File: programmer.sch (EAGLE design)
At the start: 26 parts, among them IC1 74241, U1 ATMEGA8U2, X2 SPARKFUN_USB-MICROB, Y1 16MHz

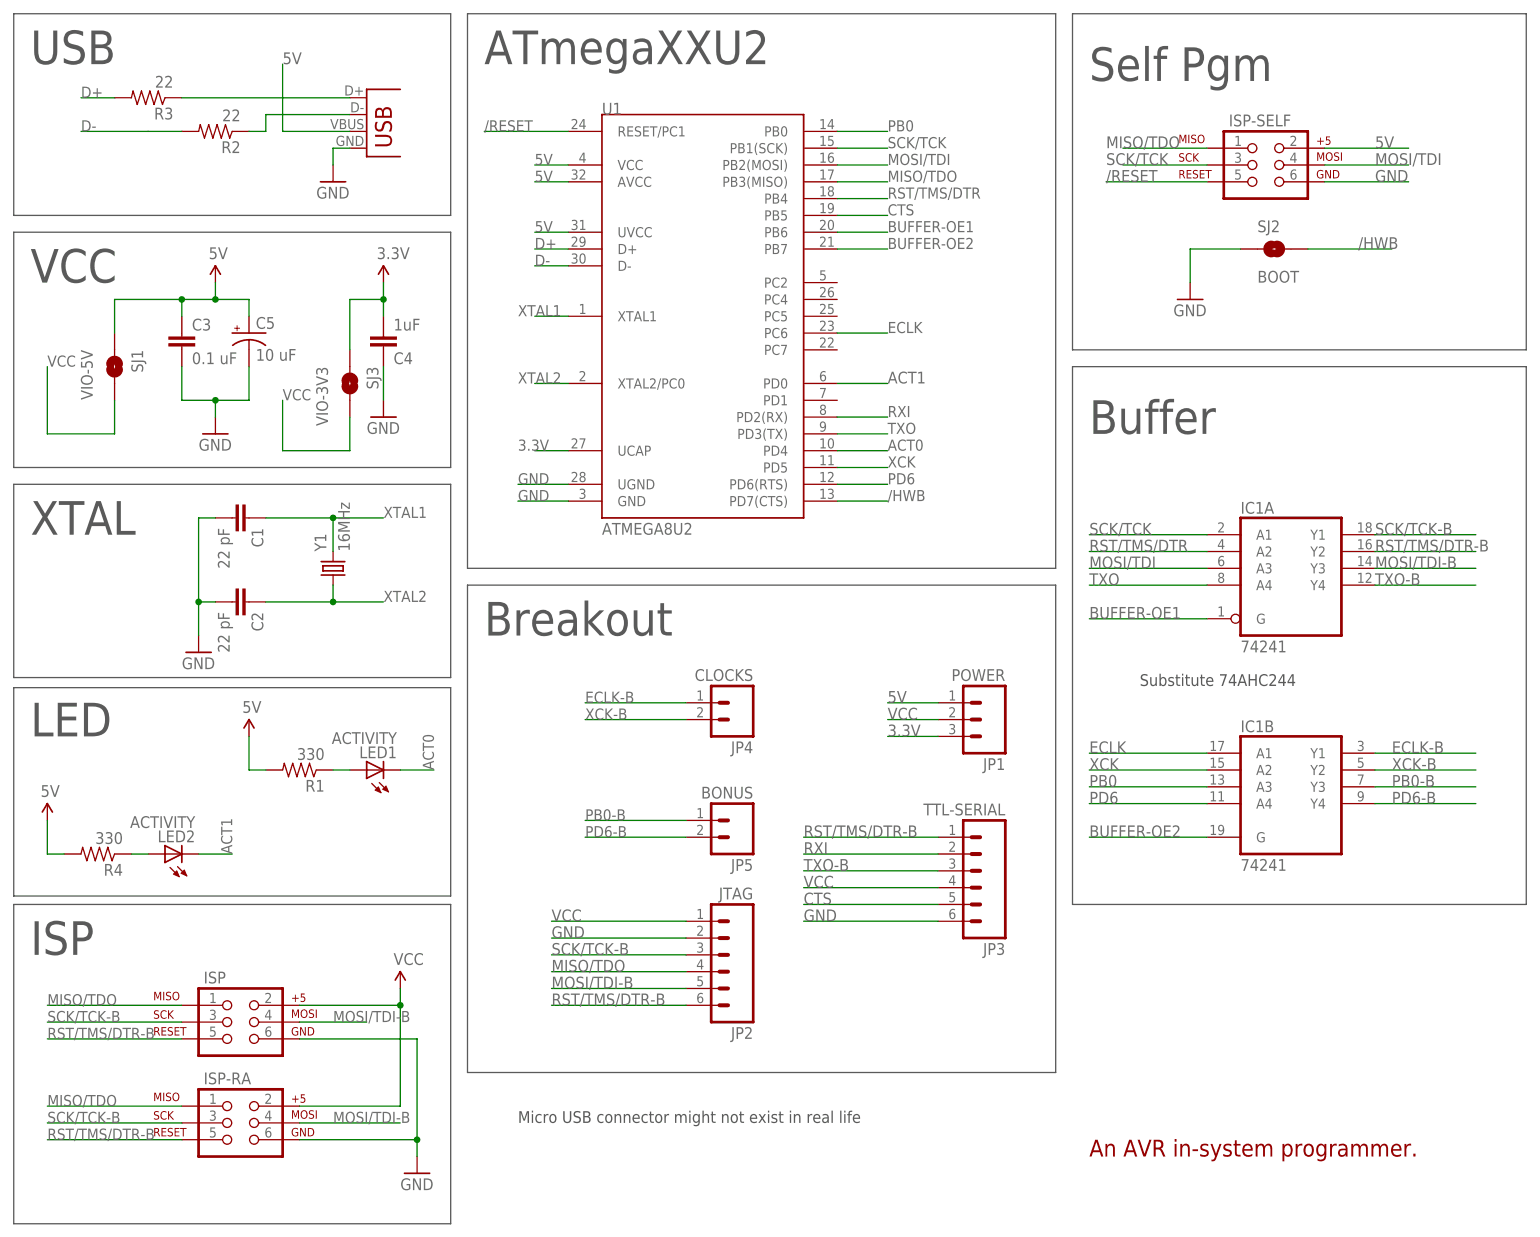
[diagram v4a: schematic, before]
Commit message: Added switch.
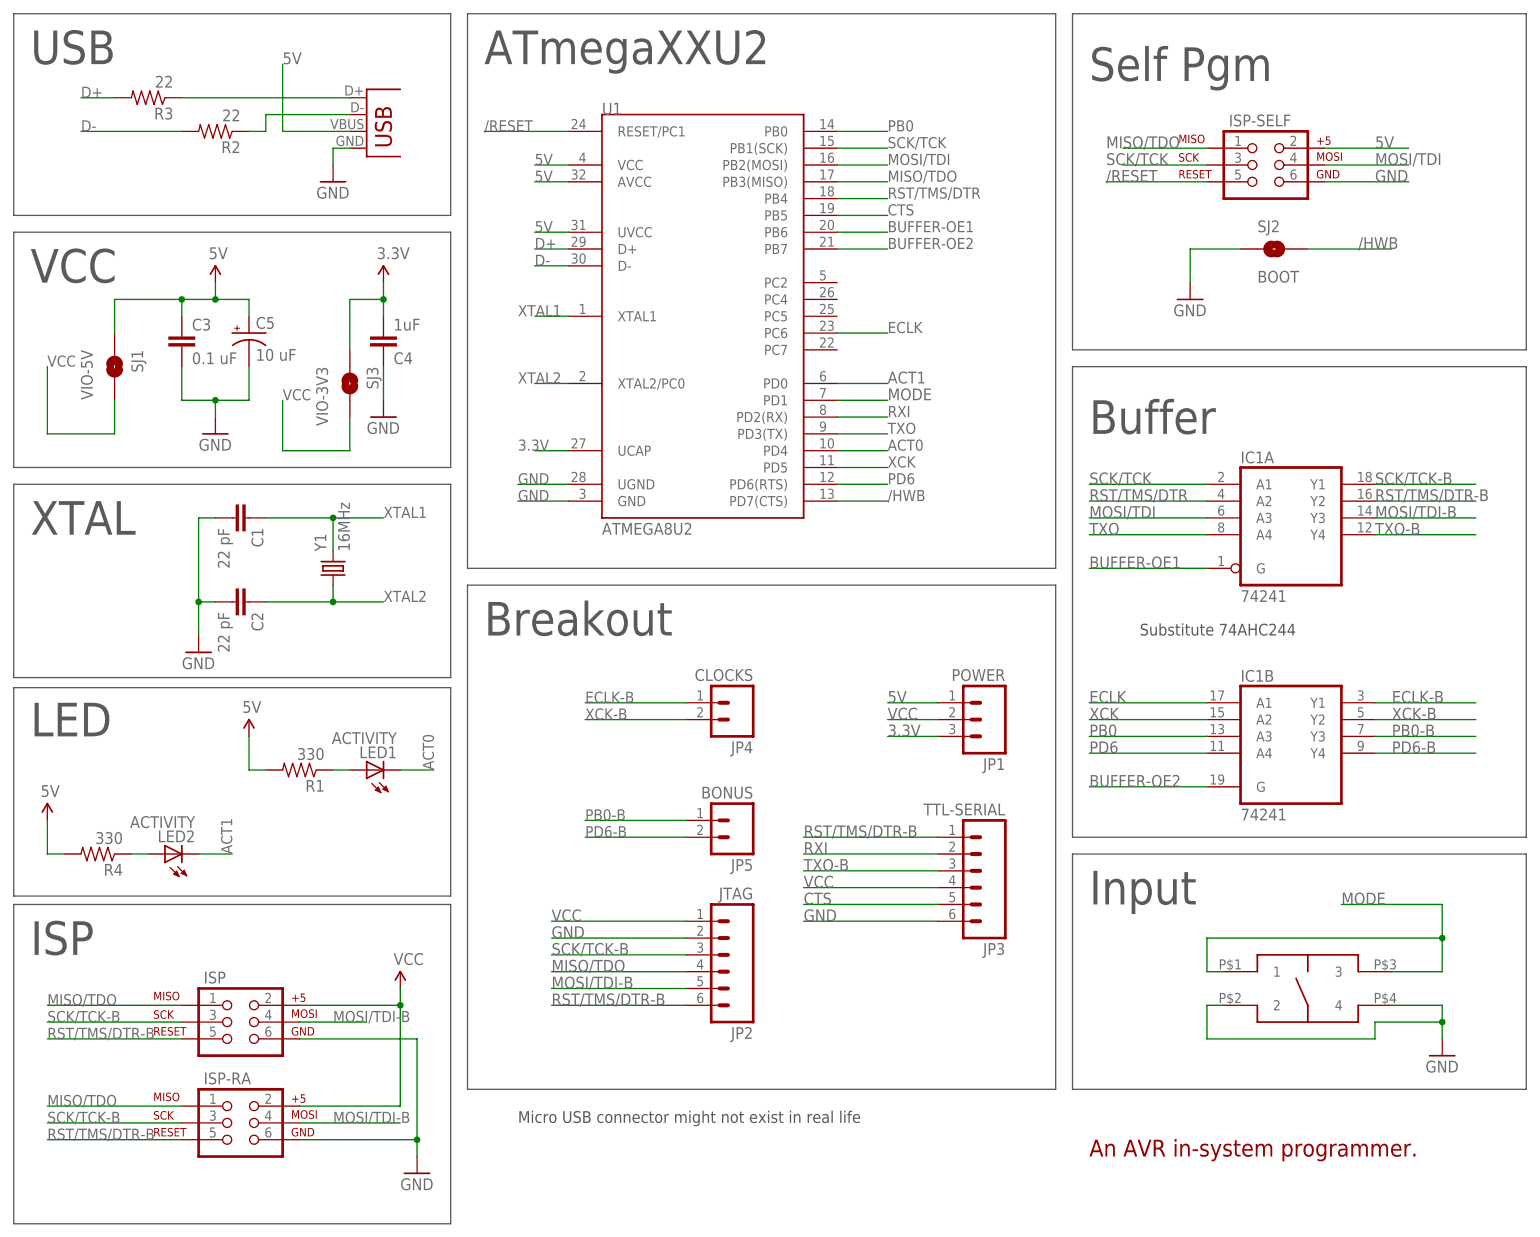
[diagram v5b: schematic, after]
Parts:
- added U$4: MOUNTAIN-MS-100625, programmer:MOUNTAIN-MS-100625
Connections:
- new net MODE: U$4.1, U$4.3, U1.PD1
- net GND: now also U$4.2, U$4.4
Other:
- note added: "Input"
- moved on the sheet: IC1A, IC1B

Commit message: Add FCI 10118193 USB socket.
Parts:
- removed X2: SPARKFUN_USB-MICROB, programmer:SPARKFUN_USB-MICROB
- added X1: FCI_8193_MICRO_USB, programmer:FCI_8193_MICRO_USB
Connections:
- net 5V: now also X1.VBUS; no longer X2.VBUS
- net D+RAW: now also X1.D+; no longer X2.D+
- net D-RAW: now also X1.D-; no longer X2.D-
- net GND: now also X1.GND; no longer X2.GND
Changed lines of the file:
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@@
 <part name="ISP-RA" library="programmer" deviceset="SPARKFUN_AVR_SPI_PRG_6" device="2X3_LOCK" value=""/>
 <part name="ISP-SELF" library="programmer" deviceset="SPARKFUN_AVR_SPI_PRG_6" device="2X3_LOCK" value=""/>
-<part name="X2" library="programmer" deviceset="SPARKFUN_USB" device="-MICROB"/>
 <part name="SJ1" library="programmer" deviceset="SPARKFUN_SOLDERJUMPER" device="NC" value="VIO-5V"/>
 <part name="JP2" library="programmer" deviceset="SPARKFUN_M06" device="LOCK" value="JTAG"/>
@@
 <part name="U$4" library="programmer" deviceset="MOUNTAIN-MS-100625" device=""/>
 <part name="GND7" library="SparkFun" deviceset="GND" device=""/>
+<part name="X1" library="programmer" deviceset="FCI_8193_MICRO_USB" device=""/>
 </parts>
 <sheets>
@@
 <instance part="ISP-RA" gate="G$1" x="-27.94" y="-27.94"/>
 <instance part="ISP-SELF" gate="G$1" x="127" y="116.84"/>
-<instance part="X2" gate="G$1" x="-7.62" y="119.38"/>
 <instance part="SJ1" gate="1" x="-45.72" y="86.36" rot="R270"/>
 <instance part="JP2" gate="G$1" x="45.72" y="-2.54" rot="R180"/>
@@
 <instance part="U$4" gate="G$1" x="134.62" y="-7.62"/>
 <instance part="GND7" gate="1" x="154.94" y="-17.78"/>
+<instance part="X1" gate="G$1" x="-5.334" y="123.19"/>
 </instances>
 <busses>
@@
 <wire x1="-10.16" y1="119.38" x2="-12.7" y2="119.38" width="0.1524" layer="91"/>
 <wire x1="-12.7" y1="119.38" x2="-12.7" y2="116.84" width="0.1524" layer="91"/>
-<pinref part="X2" gate="G$1" pin="GND"/>
+<pinref part="X1" gate="G$1" pin="GND"/>
 </segment>
 <segment>
@@
 <net name="D+RAW" class="0">
 <segment>
+<pinref part="R3" gate="G$1" pin="1"/>
+<pinref part="X1" gate="G$1" pin="D+"/>
 <wire x1="-10.16" y1="127" x2="-35.56" y2="127" width="0.1524" layer="91"/>
-<pinref part="R3" gate="G$1" pin="1"/>
-<pinref part="X2" gate="G$1" pin="D+"/>
 </segment>
 </net>
@@
 <wire x1="-22.86" y1="124.46" x2="-22.86" y2="121.92" width="0.1524" layer="91"/>
 <wire x1="-22.86" y1="121.92" x2="-25.4" y2="121.92" width="0.1524" layer="91"/>
-<pinref part="X2" gate="G$1" pin="D-"/>
+<pinref part="X1" gate="G$1" pin="D-"/>
 </segment>
 </net>
@@
 <wire x1="-20.32" y1="121.92" x2="-20.32" y2="132.08" width="0.1524" layer="91"/>
 <label x="-20.32" y="132.08" size="1.778" layer="95" font="vector"/>
-<pinref part="X2" gate="G$1" pin="VBUS"/>
-</segment>
-<segment>
+<pinref part="X1" gate="G$1" pin="VBUS"/>
+</segment>
+<segment>
